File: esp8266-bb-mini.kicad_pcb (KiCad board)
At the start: 2 copper layers, 34.3 x 31.8 mm, 21 parts, among them J1 Conn_01x04_Male, J2 Conn_01x04_Male, J3 Conn_01x04_Male, J4 Conn_01x04_Male, J5 Conn_01x02_Male, U1 LP38693MP-3.3, U2 ESP-12F

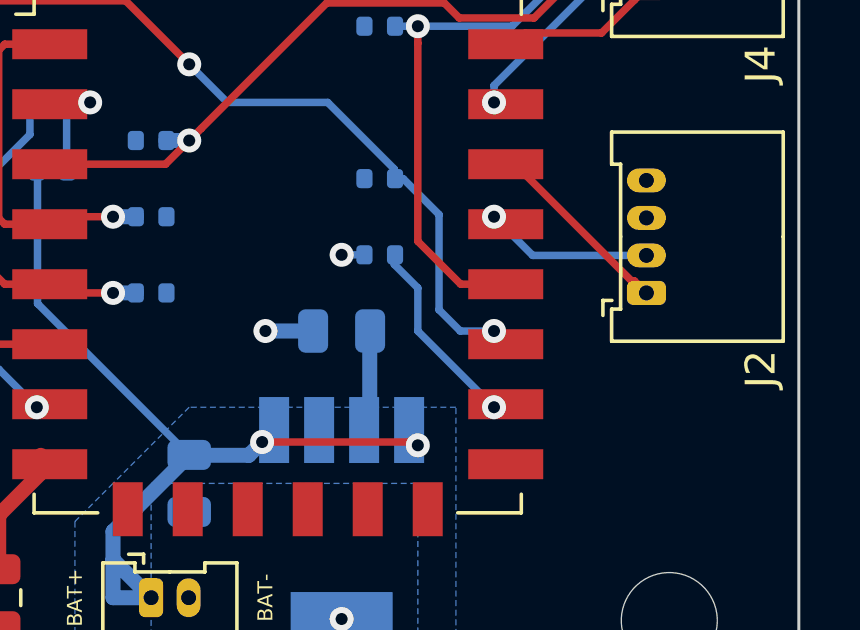
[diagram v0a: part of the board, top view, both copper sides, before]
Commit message: brd: improve routing for better connected copper pour on 3v3 plane
Signed-off-by: Tillmann Heidsieck <theidsieck@leenox.de>
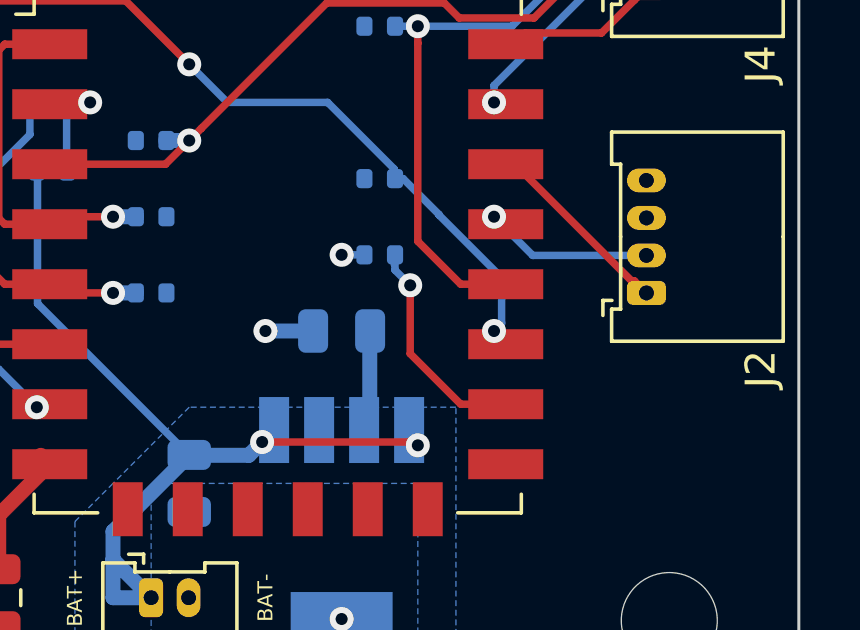
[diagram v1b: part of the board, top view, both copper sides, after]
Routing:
- net /EXT_GPIO15: track 6.46 -> 7.71 mm

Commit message: brd: add oshw logo
Signed-off-by: Tillmann Heidsieck <theidsieck@leenox.de>
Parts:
- added REF**: OSHW-Logo2_7.3x6mm_SilkScreen, Symbol:OSHW-Logo2_7.3x6mm_SilkScreen, B.Cu at (120.7, 113.5)

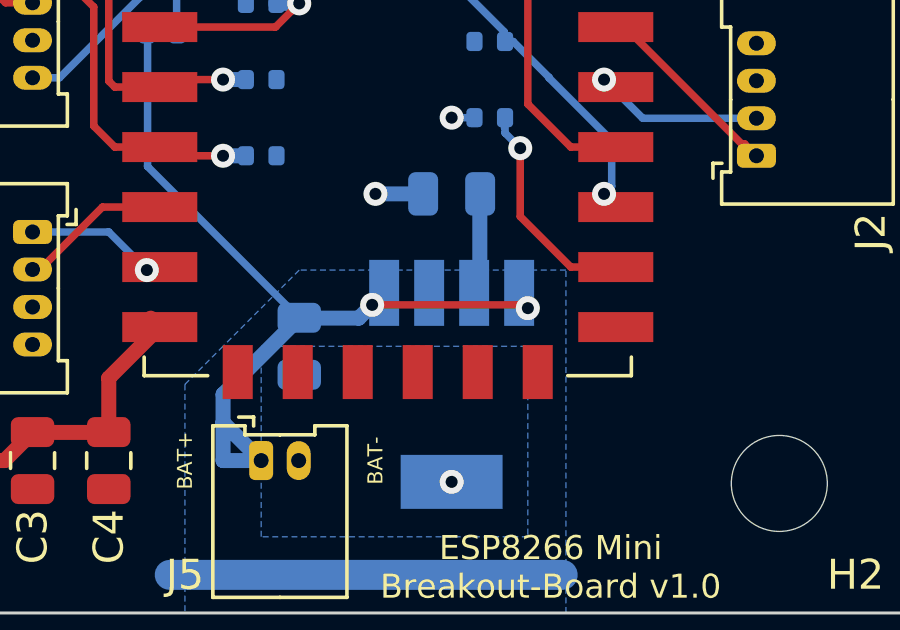
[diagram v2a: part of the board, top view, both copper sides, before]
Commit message: brd: improve copper pour on gnd plane
Signed-off-by: Tillmann Heidsieck <theidsieck@leenox.de>
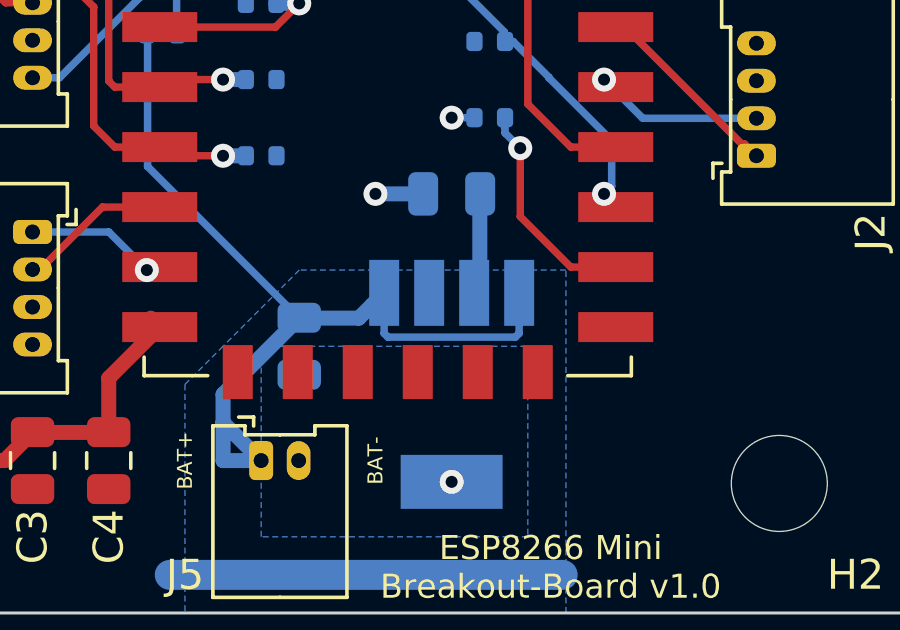
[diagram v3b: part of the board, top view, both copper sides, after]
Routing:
- net +BATT: track 28.9 -> 31.0 mm, vias 2 -> 0
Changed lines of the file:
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@@
     (thickness 1.6002)
     (drawings 28)
-    (tracks 138)
+    (tracks 139)
     (zones 0)
     (modules 22)
@@
   (segment (start 122.82 100.27) (end 121.92 100.27) (width 0.25) (layer Back) (net 1))
   (segment (start 125.499 96.52) (end 125.499 97.591) (width 0.25) (layer Back) (net 1))
-  (via (at 138.43 107.95) (size 0.8) (drill 0.4) (layers Front Back) (net 2))
   (segment (start 132.7975 108.2825) (end 133.24 107.84) (width 0.5) (layer Back) (net 2))
   (segment (start 130.81 108.2825) (end 132.7975 108.2825) (width 0.5) (layer Back) (net 2))
@@
   (segment (start 129.54 113.03) (end 128.27 113.03) (width 0.5) (layer Back) (net 2))
   (segment (start 133.24 107.84) (end 133.64 107.44) (width 0.5) (layer Back) (net 2))
-  (via (at 133.24 107.84) (size 0.8) (drill 0.4) (layers Front Back) (net 2))
-  (segment (start 138.32 107.84) (end 138.43 107.95) (width 0.25) (layer Front) (net 2))
-  (segment (start 133.24 107.84) (end 138.32 107.84) (width 0.25) (layer Front) (net 2))
   (segment (start 133.604 107.404) (end 133.64 107.44) (width 0.25) (layer Back) (net 2))
   (segment (start 125.753 103.2255) (end 130.81 108.2825) (width 0.25) (layer Back) (net 2))
   (segment (start 125.753 98.806) (end 125.753 103.2255) (width 0.25) (layer Back) (net 2))
+  (segment (start 138.014999 108.915001) (end 138.14 108.79) (width 0.25) (layer Back) (net 2))
+  (segment (start 133.765001 108.915001) (end 138.014999 108.915001) (width 0.25) (layer Back) (net 2))
+  (segment (start 133.64 108.79) (end 133.765001 108.915001) (width 0.25) (layer Back) (net 2))
+  (segment (start 138.14 108.79) (end 138.14 107.44) (width 0.25) (layer Back) (net 2))
+  (segment (start 133.64 107.44) (end 133.64 108.79) (width 0.25) (layer Back) (net 2))
   (segment (start 136.8275 107.2525) (end 136.64 107.44) (width 0.5) (layer Back) (net 3))
   (segment (start 136.8275 104.14) (end 136.8275 104.14) (width 0.5) (layer Back) (net 3))

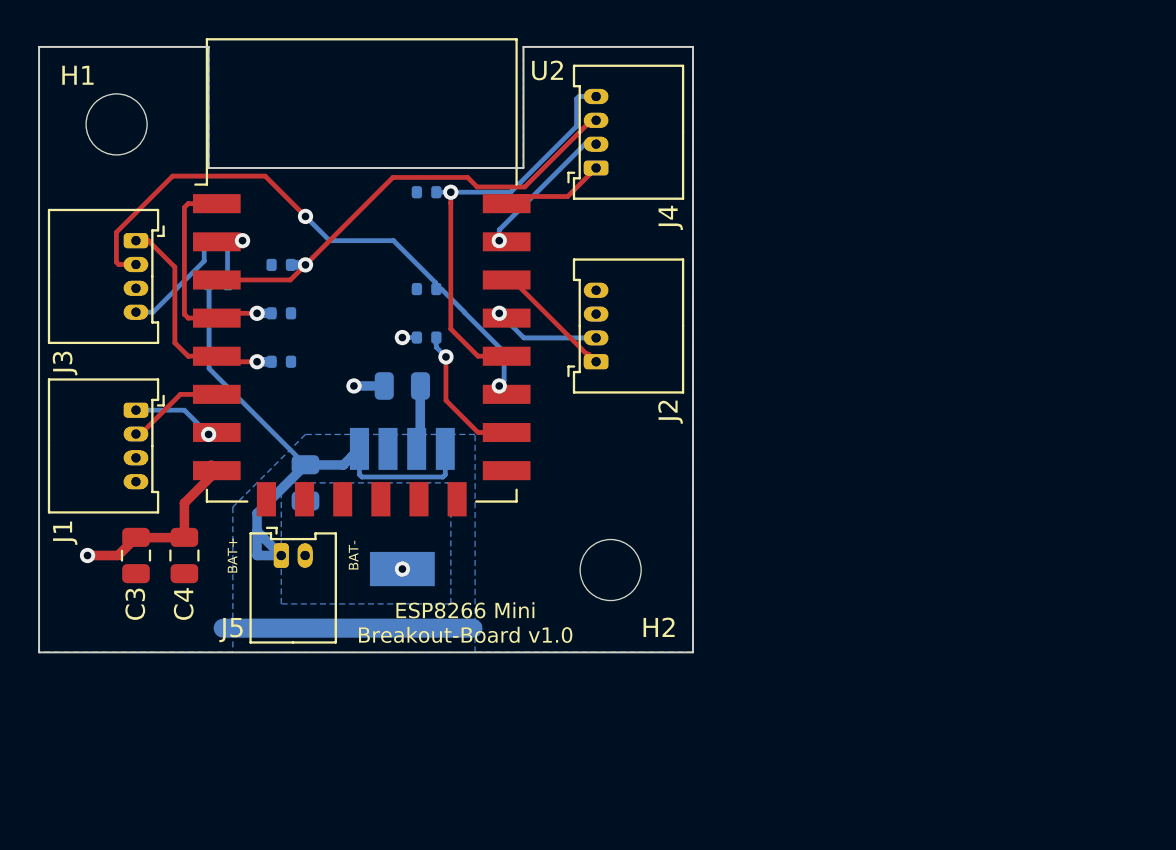
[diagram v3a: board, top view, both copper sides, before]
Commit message: new layout with bigger connectors
Signed-off-by: Tillmann Heidsieck <theidsieck@leenox.de>
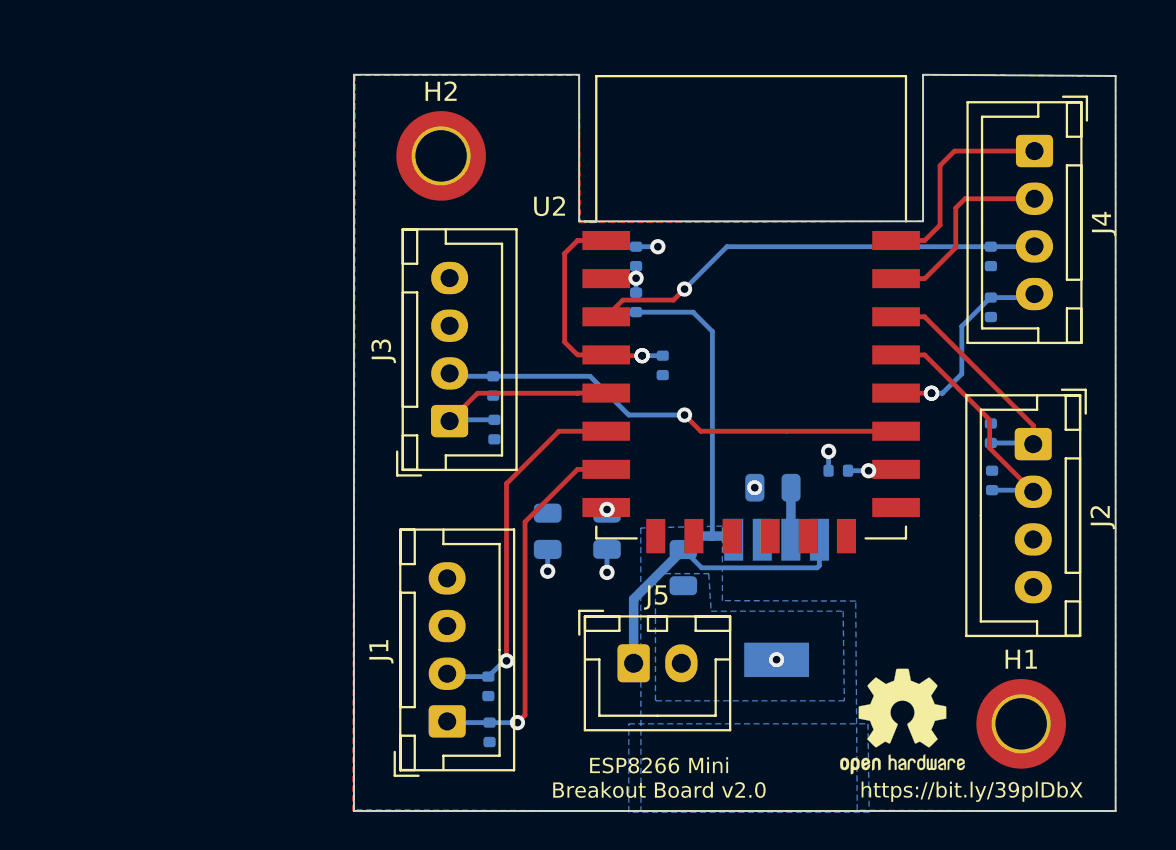
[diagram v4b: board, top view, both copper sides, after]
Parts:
- added R10: 10k, Resistor_SMD:R_0402_1005Metric, B.Cu at (140.4, 119.9)
- added R11: 10k, Resistor_SMD:R_0402_1005Metric, B.Cu at (140.5, 122.3)
- added R12: 10k, Resistor_SMD:R_0402_1005Metric, B.Cu at (140.7, 106.4)
- added R9: 10k, Resistor_SMD:R_0402_1005Metric, B.Cu at (166.8, 106.6)
- added REF**: KiCad-Logo2_5mm_SilkScreen, Symbol:KiCad-Logo2_5mm_SilkScreen, B.Cu at (159.0, 122.9)
- C3, C4: moved to B.Cu
- H1, H2: footprint MountingHole:MountingHole_3.2mm_M3 -> MountingHole:MountingHole_2.7mm_M2.5_DIN965_Pad_TopOnly
- J1, J2, J3, J4: footprint Connector_Molex:Molex_PicoBlade_53048-0410_1x04_P1.25mm_Horizontal -> Connector_JST:JST_XH_B4B-XH-A_1x04_P2.50mm_Vertical
- J5: footprint Connector_Molex:Molex_PicoBlade_53048-0210_1x02_P1.25mm_Horizontal -> Connector_JST:JST_XH_B2B-XH-A_1x02_P2.50mm_Vertical
- REF**: moved to F.Cu
- moved H1 56.9 mm to (168.3, 121.9)
- moved REF** 42.3 mm to (162.1, 121.7), turned to 0 degrees
- moved R8 37.8 mm to (166.8, 109.1), turned to 270 degrees
- moved R1 37.2 mm to (166.8, 97.3), turned to 90 degrees
- moved R6 29.6 mm to (166.8, 100.0), turned to 90 degrees
- moved R5 26.1 mm to (158.8, 108.6)
- moved H2 23.5 mm to (137.9, 92.1)
- moved J2 23.3 mm to (169.0, 107.2), turned to 270 degrees
- moved J1 23.1 mm to (138.2, 121.7), turned to 90 degrees
- moved J4 23.0 mm to (169.0, 91.8), turned to 270 degrees
- moved C4 22.2 mm to (146.6, 111.8)
- moved R4 22.2 mm to (148.1, 97.3), turned to 90 degrees
- moved R3 21.9 mm to (148.1, 99.8), turned to 90 degrees
- moved C3 21.6 mm to (143.5, 111.8)
- moved U2 20.5 mm to (154.2, 100.0)
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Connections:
- R5 pad 1: /EXT_GPIO0 -> /EXT_GPIO15
- R5 pad 2: +3V3 -> -BATT
- R6 pad 1: /EXT_GPIO15 -> +3V3
- R6 pad 2: -BATT -> /EXT_GPIO0
- R8 pad 2: /EXT_GPIO14 -> /EXT_GPIO4
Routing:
- net +3V3: track 26.8 -> 2.73 mm
- net /EXT_GPIO13: track 4.34 -> 19.9 mm
- net /EXT_GPIO12: track 4.88 -> 19.2 mm, vias 0 -> 1
- net /EXT_GPIO0: track 22.0 -> 10.9 mm, vias 1 -> 2
- net /EXT_GPIO4: track 5.61 -> 13.3 mm, vias 1 -> 0
- net /EXT_GPIO5: track 6.47 -> 12.9 mm
- net /EXT_TXD: track 5.46 -> 11.0 mm
- net /EXT_GPIO2: track 30.1 -> 24.9 mm, vias 2 -> 1
- net /EXT_GPIO15: track 7.71 -> 2.55 mm
- net -BATT: track 8.15 -> 4.64 mm, vias 3 -> 6
- net +BATT: track 31.0 -> 34.1 mm
- net /EXT_RXD: track 7.52 -> 10.2 mm, vias 1 -> 0
- net /ADC_IN: track 4.80 -> 2.99 mm
- net /EXT_GPIO14: track 12.1 -> 11.3 mm, vias 1 -> 0
- net /nRST: track 12.2 -> 12.6 mm, vias 1 -> 2
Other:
- board size 34.3 x 31.8 mm -> 39.9 x 38.6 mm
- board text added: "ESP8266 Mini Breakout Board v2.0"
- board text added: "https://bit.ly/39plDbX"
- board text removed: "BAT+"
- board text removed: "BAT-"
- board text removed: "ESP8266 Mini Breakout-Board v1.0"
- board text removed: "Source under https://bit.ly/39piDbX"

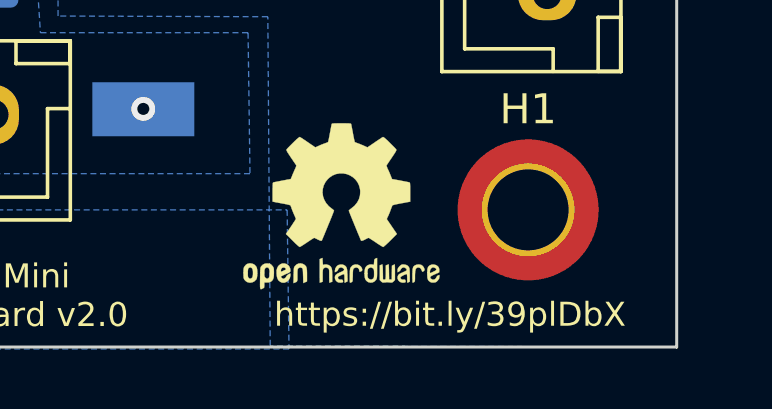
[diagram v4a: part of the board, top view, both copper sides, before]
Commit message: pcb: fix https link on silk
Signed-off-by: Tillmann Heidsieck <theidsieck@leenox.de>
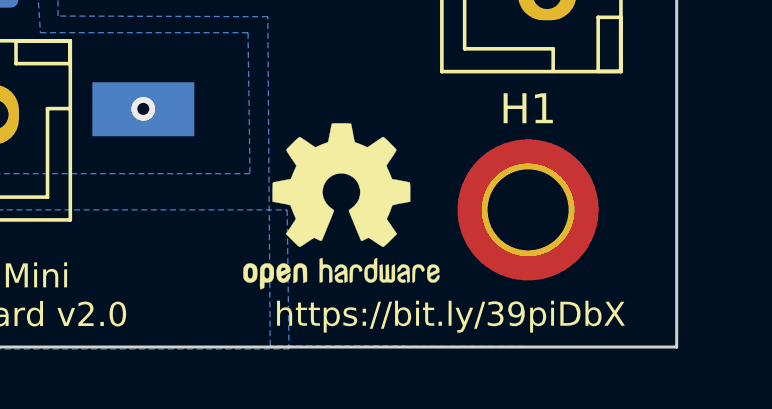
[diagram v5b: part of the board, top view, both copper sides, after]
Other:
- board text added: "https://bit.ly/39piDbX"
- board text removed: "https://bit.ly/39plDbX"
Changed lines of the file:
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@@
     )
   )
-  (gr_text https://bit.ly/39plDbX (at 165.735 125.349) (layer F.SilkS)
+  (gr_text https://bit.ly/39piDbX (at 165.735 125.349) (layer F.SilkS)
     (effects (font (size 0.8 0.8) (thickness 0.1)))
   )
@@
     (connect_pads (clearance 0.508))
     (min_thickness 0.254)
-    (fill (arc_segments 32) (thermal_gap 0.508) (thermal_bridge_width 0.508))
+    (fill yes (arc_segments 32) (thermal_gap 0.508) (thermal_bridge_width 0.508))
     (polygon
       (pts
@@
     (connect_pads (clearance 0.508))
     (min_thickness 0.254)
-    (fill (arc_segments 32) (thermal_gap 0.508) (thermal_bridge_width 0.508))
+    (fill yes (arc_segments 32) (thermal_gap 0.508) (thermal_bridge_width 0.508))
     (polygon
       (pts
@@
     (connect_pads (clearance 0.508))
     (min_thickness 0.254)
-    (fill (arc_segments 32) (thermal_gap 0.508) (thermal_bridge_width 0.508))
+    (fill yes (arc_segments 32) (thermal_gap 0.508) (thermal_bridge_width 0.508))
     (polygon
       (pts
@@
     (connect_pads (clearance 0.508))
     (min_thickness 0.254)
-    (fill (arc_segments 32) (thermal_gap 0.508) (thermal_bridge_width 0.508))
-    (polygon
-      (pts
+    (fill yes (arc_segments 32) (thermal_gap 0.508) (thermal_bridge_width 0.508))
+    (polygon
+      (pts
